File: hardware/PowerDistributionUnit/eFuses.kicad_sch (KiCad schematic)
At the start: 10 parts, among them U3 TCA9544A, U32 ADS7953SBDBT

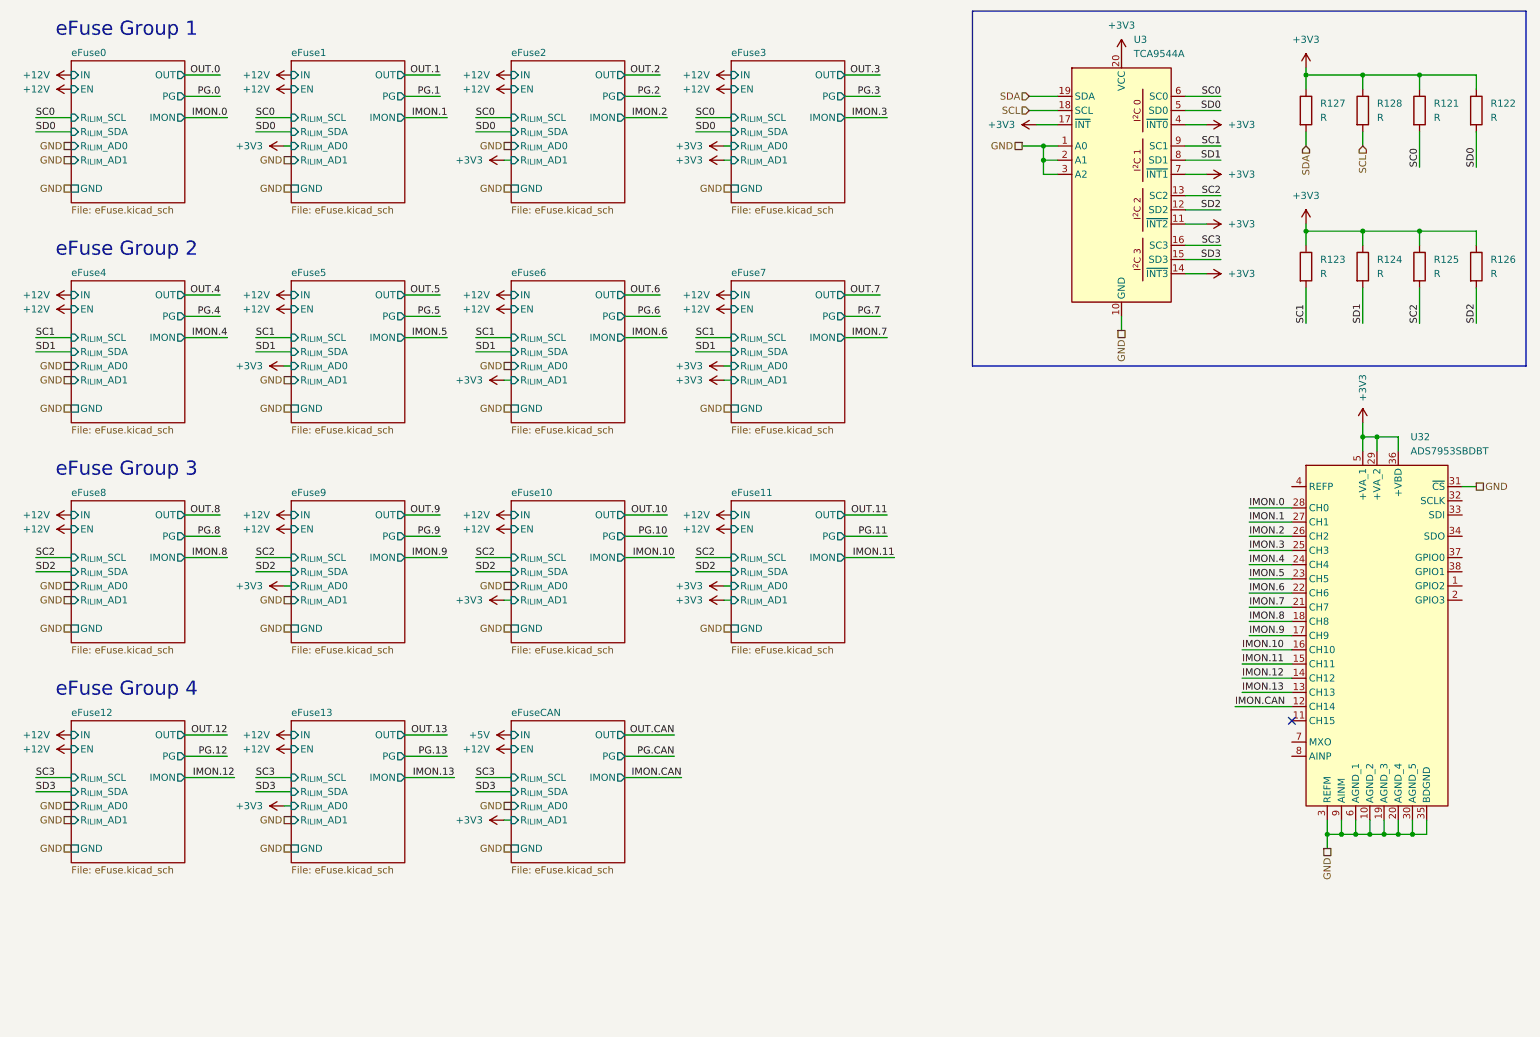
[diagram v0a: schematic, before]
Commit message: split off monitoring to its own sheet, continued connecting hardware and adding symbols
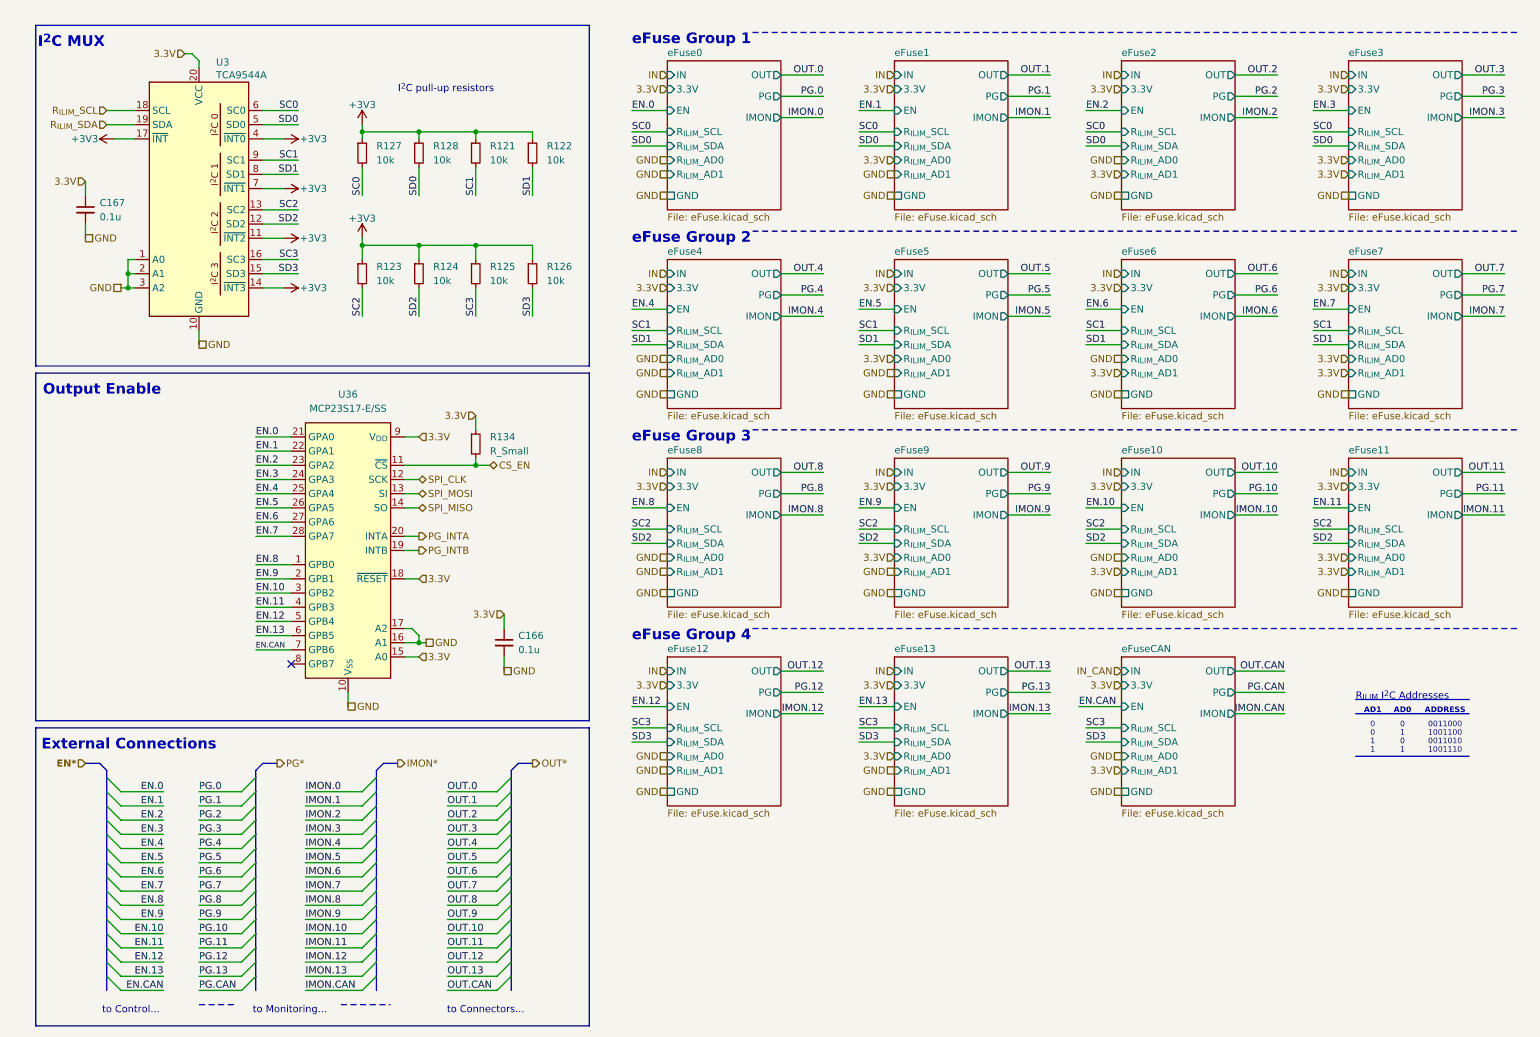
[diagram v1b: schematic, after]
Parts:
- removed U32: ADS7953SBDBT, symbol PowerDistributionUnitLib:ADS7953SBDBT
- added C166, C167: 0.1u, symbol Device:C_Small
- added R134: R_Small, symbol Device:R_Small
- added U36: MCP23S17-E/SS, Package_SO:SSOP-28_5.3x10.2mm_P0.65mm, symbol PowerDistributionUnitLib:MCP23S17-E/SS
- R121, R122, R123, R124, R125, R126, R127, R128: value R -> 10k; symbol Device:R -> Device:R_Small
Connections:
- net +3V3: no longer U3.20 (VCC)
- net GND: now also C166.2, C167.2, U36.10 (V_{SS}), U36.16 (A1), U36.17 (A2)
- net SC0: now also R127.2; no longer R121.2
- net SC1: now also R121.2; no longer R123.2
- net SC2: now also R123.2; no longer R125.2
- net SC3: now also R125.2
- net SD0: now also R128.2; no longer R122.2
- net SD1: now also R122.2; no longer R124.2
- net SD2: now also R124.2; no longer R126.2
- net SD3: now also R126.2
- net SCL renamed R_{ILIM}_SCL
- net R_{ILIM}_SCL: no longer R128.2
- net SDA renamed R_{ILIM}_SDA
- net R_{ILIM}_SDA: no longer R127.2
- new net 3.3V: C166.1, C167.1, R134.1, U3.20 (VCC), U36.15 (A0), U36.18 (~{RESET}), U36.9 (V_{DD})
- new net CS_EN: R134.2, U36.11 (~{CS})
- new net EN.0: U36.21 (GPA0)
- new net EN.1: U36.22 (GPA1)
- new net EN.10: U36.3 (GPB2)
- new net EN.11: U36.4 (GPB3)
- new net EN.12: U36.5 (GPB4)
- new net EN.13: U36.6 (GPB5)
- new net EN.2: U36.23 (GPA2)
- new net EN.3: U36.24 (GPA3)
- new net EN.4: U36.25 (GPA4)
- new net EN.5: U36.26 (GPA5)
- new net EN.6: U36.27 (GPA6)
- new net EN.7: U36.28 (GPA7)
- new net EN.8: U36.1 (GPB0)
- new net EN.9: U36.2 (GPB1)
- new net EN.CAN: U36.7 (GPB6)
- new net PG_INTA: U36.20 (INTA)
- new net PG_INTB: U36.19 (INTB)
- new net SPI_CLK: U36.12 (SCK)
- new net SPI_MISO: U36.14 (SO)
- new net SPI_MOSI: U36.13 (SI)
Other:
- sheet eFuse0 ports: added 3.3V; removed none
- sheet eFuse1 ports: added 3.3V; removed none
- sheet eFuse10 ports: added 3.3V; removed none
- sheet eFuse11 ports: added 3.3V; removed none
- sheet eFuse12 ports: added 3.3V; removed none
- sheet eFuse13 ports: added 3.3V; removed none
- sheet eFuse2 ports: added 3.3V; removed none
- sheet eFuse3 ports: added 3.3V; removed none
- sheet eFuse4 ports: added 3.3V; removed none
- sheet eFuse5 ports: added 3.3V; removed none
- sheet eFuse6 ports: added 3.3V; removed none
- sheet eFuse7 ports: added 3.3V; removed none
- sheet eFuse8 ports: added 3.3V; removed none
- sheet eFuse9 ports: added 3.3V; removed none
- sheet eFuseCAN ports: added 3.3V; removed none
- note added: "0"
- note added: "0011000"
- note added: "0011010"
- note added: "1"
- note added: "1001100"
- note added: "1001110"
- note added: "AD0"
- note added: "AD1"
- note added: "ADDRESS"
- note added: "External Connections"
- note added: "I^{2}C MUX"
- note added: "I^{2}C pull-up resistors"
- note added: "Output Enable"
- note added: "R_{ILIM} I^{2}C Addresses"
- note added: "to Connectors..."
- note added: "to Control..."
- note added: "to Monitoring..."
- moved on the sheet: R121, R122, R123, R124, R125, R126, R127, R128, U3

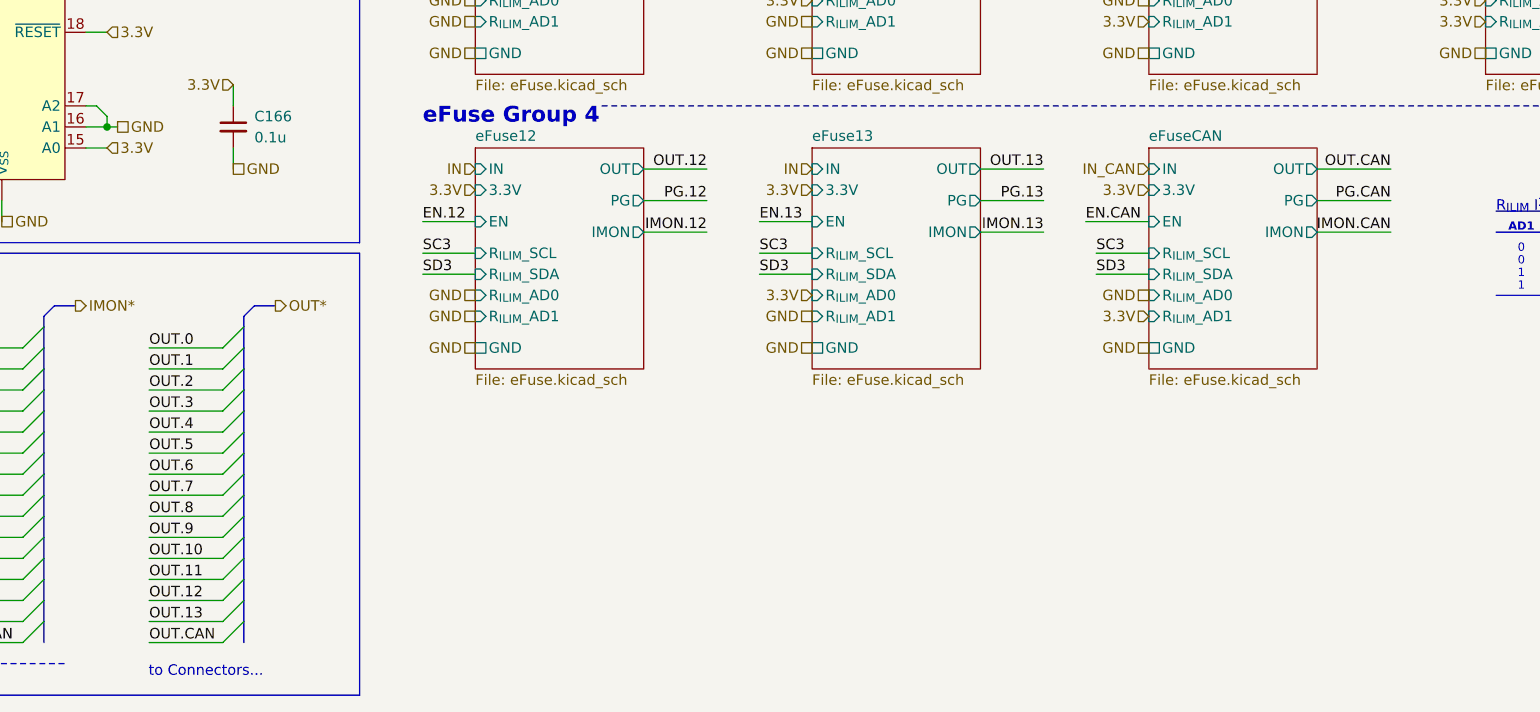
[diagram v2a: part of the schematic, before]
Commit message: added isolated CAN 5V DC-DC converter, updated power netclasses
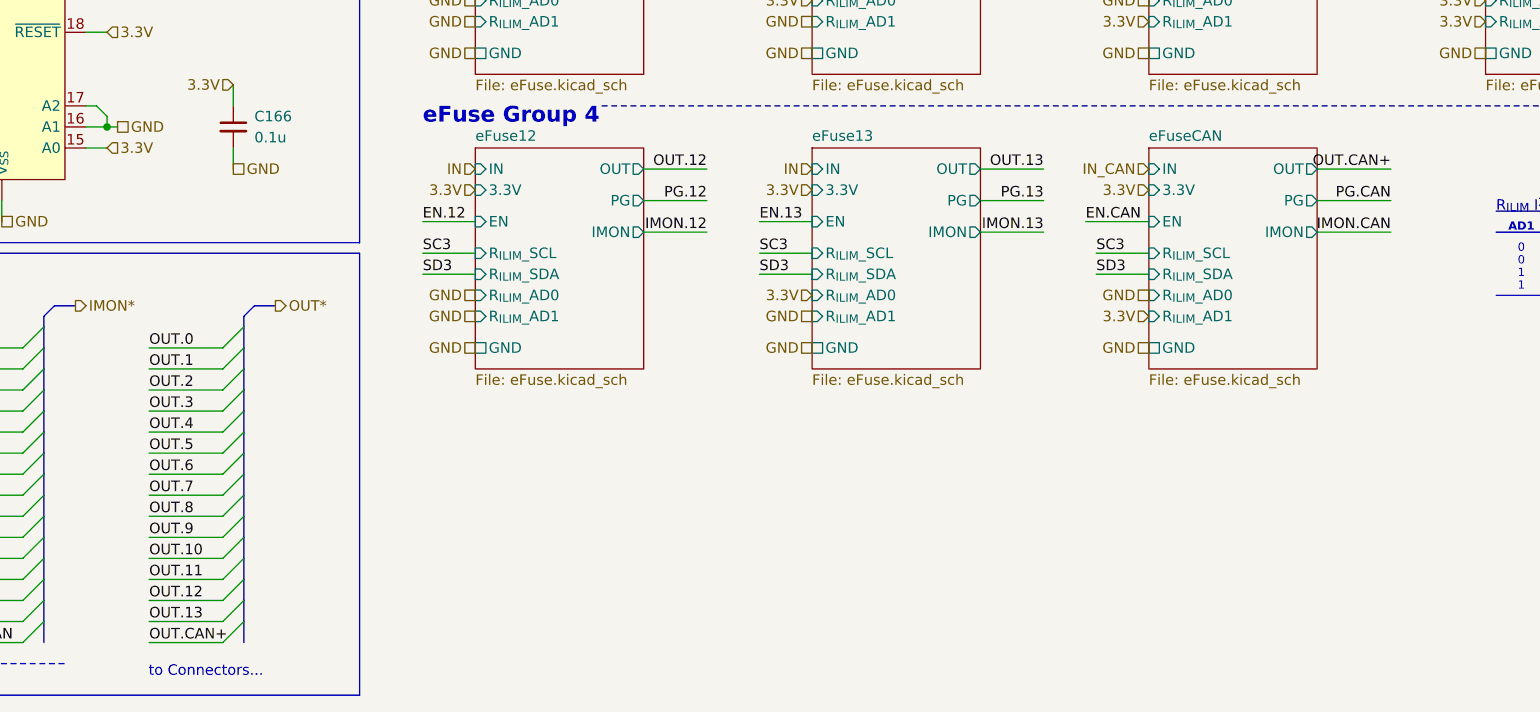
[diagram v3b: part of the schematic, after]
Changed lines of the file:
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@@
 		)
 	)
-	(label "OUT.CAN"
+	(label "OUT.CAN+"
 		(at 240.03 130.81 180)
 		(fields_autoplaced yes)
@@
 		)
 	)
-	(label "OUT.CAN"
+	(label "OUT.CAN+"
 		(at 90.17 187.96 0)
 		(fields_autoplaced yes)

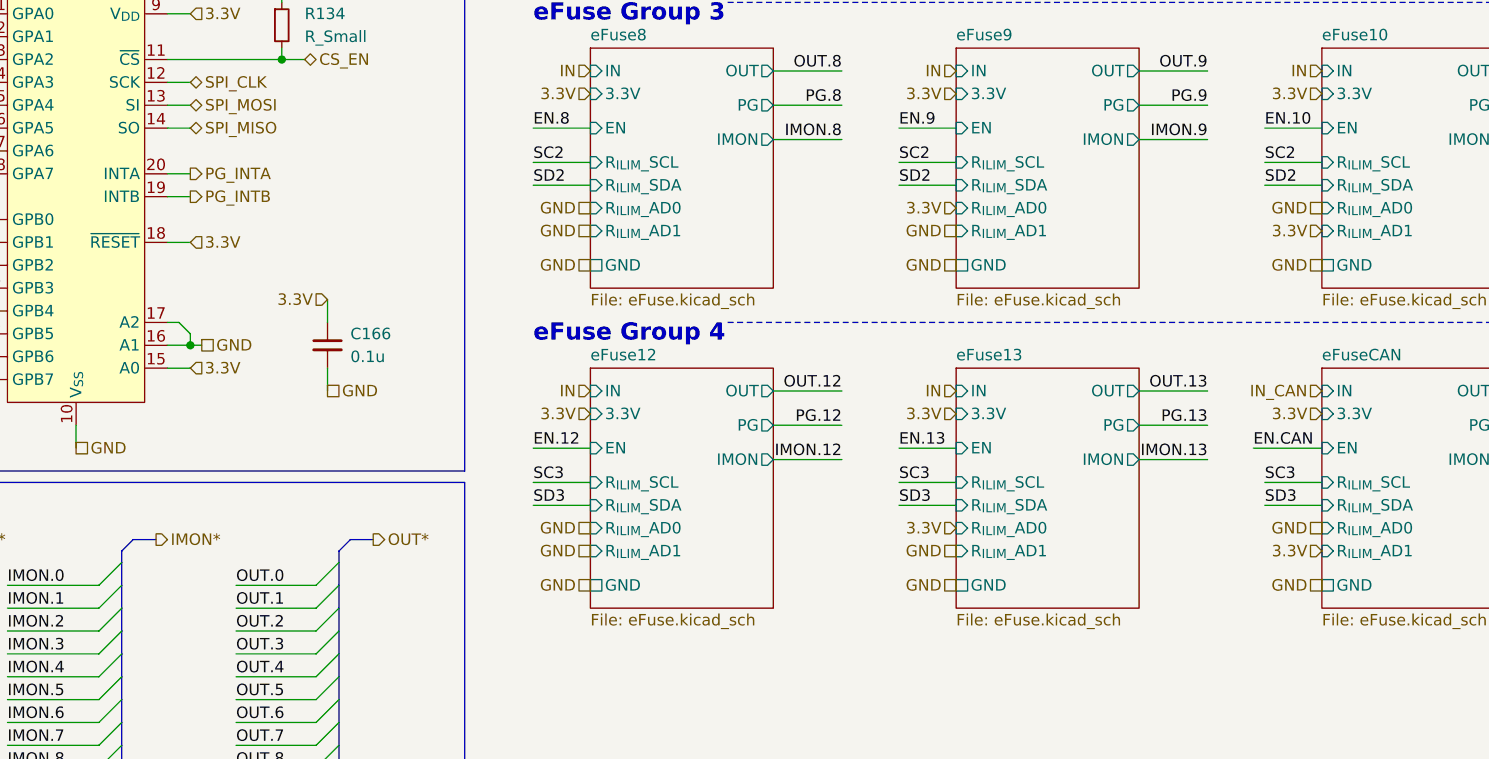
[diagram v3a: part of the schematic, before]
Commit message: fixed Lakshay review things (CAN DC-DC output caps, DC-DC symbol name update, fix CAN eFuse isolation, add CAN connectors, DC-DC RC jumper, voltage label) and removed PG int from EN mux
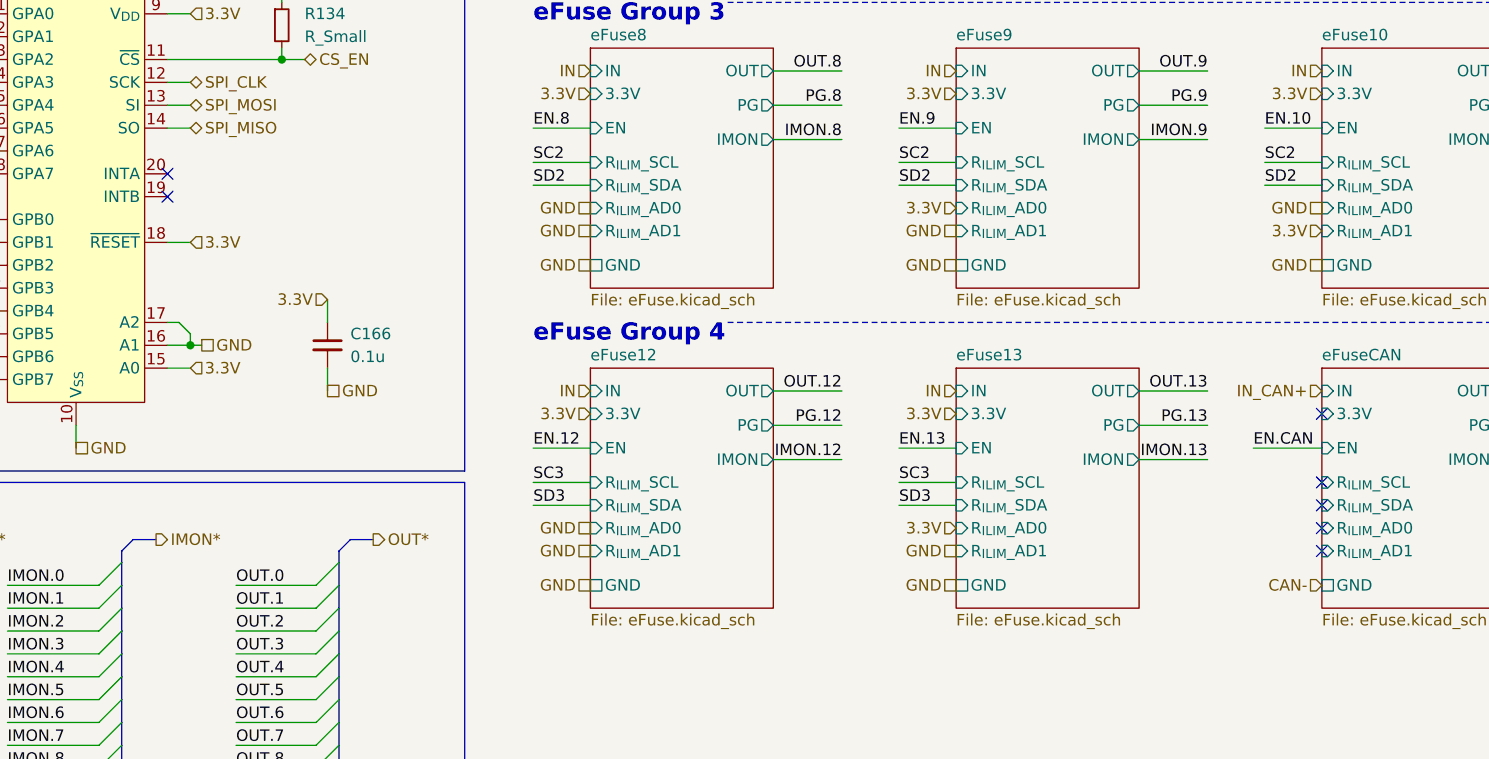
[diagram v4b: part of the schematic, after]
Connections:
- net PG_INTA: no longer names the net of U36.20 (INTA)
- net PG_INTB: no longer names the net of U36.19 (INTB)
- no-connect marks 1 -> 8
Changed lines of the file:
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@@
 	)
 	(no_connect
+		(at 210.82 148.59)
+	)
+	(no_connect
+		(at 210.82 133.35)
+	)
+	(no_connect
 		(at 62.23 129.54)
 	)
+	(no_connect
+		(at 210.82 140.97)
+	)
+	(no_connect
+		(at 82.55 106.68)
+	)
+	(no_connect
+		(at 210.82 146.05)
+	)
+	(no_connect
+		(at 82.55 109.22)
+	)
+	(no_connect
+		(at 210.82 143.51)
+	)
 	(bus_entry
 		(at 29.21 182.88)
@@
 	(wire
 		(pts
-			(xy 204.47 140.97) (xy 210.82 140.97)
-		)
-		(stroke
-			(width 0)
-			(type default)
-		)
-	)
-	(wire
-		(pts
 			(xy 60.96 62.23) (xy 57.15 62.23)
 		)
@@
 		)
 	)
-	(wire
-		(pts
-			(xy 82.55 109.22) (xy 85.09 109.22)
-		)
-		(stroke
-			(width 0)
-			(type default)
-		)
-	)
 	(bus
 		(pts
@@
 		)
 	)
-	(wire
-		(pts
-			(xy 82.55 106.68) (xy 85.09 106.68)
-		)
-		(stroke
-			(width 0)
-			(type default)
-		)
-	)
 	(bus
 		(pts
@@
 	(wire
 		(pts
-			(xy 204.47 143.51) (xy 210.82 143.51)
-		)
-		(stroke
-			(width 0)
-			(type default)
-		)
-	)
-	(wire
-		(pts
 			(xy 45.72 157.48) (xy 53.34 157.48)
 		)
@@
 		)
 	)
-	(label "SD3"
-		(at 204.47 143.51 0)
-		(fields_autoplaced yes)
-		(effects
-			(font
-				(size 1.27 1.27)
-			)
-			(justify left bottom)
-		)
-	)
 	(label "IMON.6"
 		(at 238.76 67.31 180)
@@
 		)
 	)
-	(label "SC3"
-		(at 204.47 140.97 0)
-		(fields_autoplaced yes)
-		(effects
-			(font
-				(size 1.27 1.27)
-			)
-			(justify left bottom)
-		)
-	)
 	(label "SD0"
 		(at 123.19 36.83 0)
@@
 	(hierarchical_label "GND"
 		(shape passive)
-		(at 210.82 152.4 180)
-		(fields_autoplaced yes)
-		(effects
-			(font
-				(size 1.27 1.27)
-				(color 0 0 0 1)
-			)
-			(justify right)
-		)
-	)
-	(hierarchical_label "GND"
-		(shape passive)
 		(at 170.18 116.84 180)
 		(fields_autoplaced yes)
@@
 		)
 	)
-	(hierarchical_label "PG_INTB"
-		(shape output)
-		(at 85.09 109.22 0)
-		(fields_autoplaced yes)
-		(effects
-			(font
-				(size 1.27 1.27)
-			)
-			(justify left)
-		)
-	)
 	(hierarchical_label "GND"
 		(shape passive)
@@
 		)
 	)
-	(hierarchical_label "IN_CAN"
+	(hierarchical_label "IN_CAN+"
 		(shape input)
 		(at 210.82 130.81 180)
@@
 		)
 	)
-	(hierarchical_label "3.3V"
-		(shape input)
-		(at 210.82 148.59 180)
-		(fields_autoplaced yes)
-		(effects
-			(font
-				(size 1.27 1.27)
-				(color 255 0 0 1)
-			)
-			(justify right)
-		)
-	)
 	(hierarchical_label "GND"
 		(shape passive)
@@
 		)
 	)
-	(hierarchical_label "GND"
-		(shape passive)
-		(at 210.82 146.05 180)
-		(fields_autoplaced yes)
-		(effects
-			(font
-				(size 1.27 1.27)
-				(color 0 0 0 1)
-			)
-			(justify right)
-		)
-	)
 	(hierarchical_label "3.3V"
 		(shape input)
@@
 		)
 	)
-	(hierarchical_label "PG_INTA"
-		(shape output)
-		(at 85.09 106.68 0)
-		(fields_autoplaced yes)
-		(effects
-			(font
-				(size 1.27 1.27)
-			)
-			(justify left)
-		)
-	)
 	(hierarchical_label "IN"
 		(shape input)
@@
 		)
 	)
+	(hierarchical_label "CAN-"
+		(shape input)
+		(at 210.82 152.4 180)
+		(fields_autoplaced yes)
+		(effects
+			(font
+				(size 1.27 1.27)
+				(color 0 0 0 1)
+			)
+			(justify right)
+		)
+	)
 	(hierarchical_label "IN"
 		(shape input)
@@
 		)
 	)
-	(hierarchical_label "3.3V"
-		(shape input)
-		(at 210.82 133.35 180)
-		(fields_autoplaced yes)
-		(effects
-			(font
-				(size 1.27 1.27)
-				(color 255 0 0 1)
-			)
-			(justify right)
-		)
-	)
